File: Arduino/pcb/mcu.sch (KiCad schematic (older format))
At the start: 25 parts, among them J9 FTDI, SW2 Reset Button, U2 ATMEGA328P-AU, U3 24LC64, Y1 20 Mhz Crystal

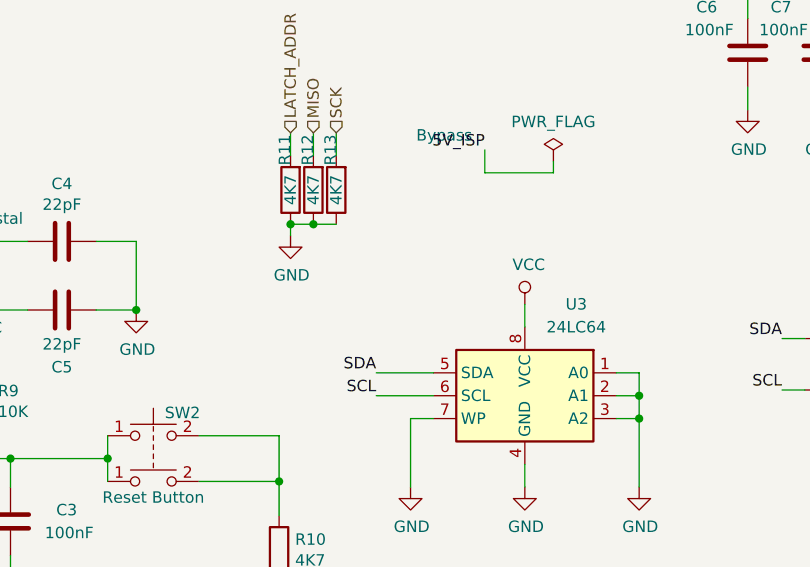
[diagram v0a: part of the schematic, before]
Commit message: pcb: mcu: add and route I2C pull up resistors
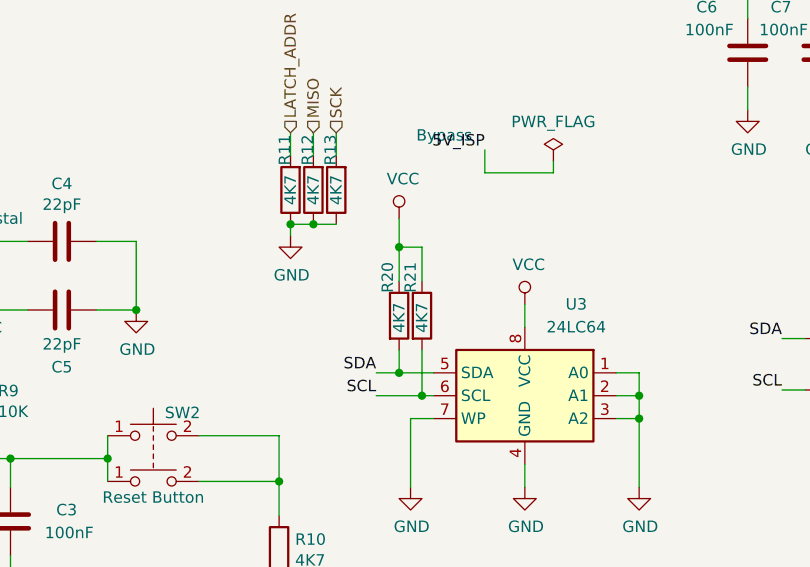
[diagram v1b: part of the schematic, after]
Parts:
- added R20, R21: 4K7, Resistor_SMD:R_0805_2012Metric, symbol Device:R
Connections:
- net SCL: now also R21.2
- net SDA: now also R20.2
- net VCC: now also R20.1, R21.1
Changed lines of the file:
@@
 RESET
 Wire Wire Line
-	8425 3550 8675 3550
-Wire Wire Line
-	8425 3650 8675 3650
+	8425 3550 8525 3550
 $Bitmap
 Pos 2000 2125
@@
 EndData
 $EndBitmap
+$Comp
+L Device:R R21
+U 1 1 5D785D49
+P 8625 3300
+F 0 "R21" V 8575 3400 50  0000 L CNN
+F 1 "4K7" V 8625 3225 50  0000 L CNN
+F 2 "Resistor_SMD:R_0805_2012Metric" V 8555 3300 50  0001 C CNN
+F 3 "~" H 8625 3300 50  0001 C CNN
+	1    8625 3300
+	1    0    0    -1
+$EndComp
+$Comp
+L Device:R R20
+U 1 1 5D78678B
+P 8525 3300
+F 0 "R20" V 8475 3400 50  0000 L CNN
+F 1 "4K7" V 8525 3225 50  0000 L CNN
+F 2 "Resistor_SMD:R_0805_2012Metric" V 8455 3300 50  0001 C CNN
+F 3 "~" H 8525 3300 50  0001 C CNN
+	1    8525 3300
+	1    0    0    -1
+$EndComp
+Wire Wire Line
+	8625 3450 8625 3650
+Connection ~ 8625 3650
+Wire Wire Line
+	8625 3650 8675 3650
+Wire Wire Line
+	8425 3650 8625 3650
+Wire Wire Line
+	8525 3450 8525 3550
+Connection ~ 8525 3550
+Wire Wire Line
+	8525 3550 8675 3550
+Wire Wire Line
+	8525 3150 8525 3000
+Wire Wire Line
+	8625 3150 8625 3000
+Wire Wire Line
+	8625 3000 8525 3000
+Wire Wire Line
+	8525 3000 8525 2875
+Connection ~ 8525 3000
+$Comp
+L power:VCC #PWR0101
+U 1 1 5D7ACF72
+P 8525 2875
+F 0 "#PWR0101" H 8525 2725 50  0001 C CNN
+F 1 "VCC" H 8542 3048 50  0000 C CNN
+F 2 "" H 8525 2875 50  0001 C CNN
+F 3 "" H 8525 2875 50  0001 C CNN
+	1    8525 2875
+	1    0    0    -1
+$EndComp
 $EndSCHEMATC

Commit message: pcb: use OR gate between FTDI and RS485 TX lines
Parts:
- added U5: 74AHCT1G32, Package_TO_SOT_SMD:SOT-23-5, symbol 74xGxx:74AHCT1G32
- R7, R8: value 100R -> 4k7
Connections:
- wire segments 109 -> 116
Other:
- moved on the sheet: C3
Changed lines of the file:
@@
 	7650 4025 8000 4025
 $Comp
-L Device:C C3
-U 1 1 5CCED101
-P 6825 4200
-F 0 "C3" H 7025 4250 50  0000 L CNN
-F 1 "100nF" H 6975 4150 50  0000 L CNN
-F 2 "Capacitor_SMD:C_0805_2012Metric" H 6863 4050 50  0001 C CNN
-F 3 "~" H 6825 4200 50  0001 C CNN
-	1    6825 4200
-	1    0    0    -1
-$EndComp
-$Comp
 L Device:R R10
 U 1 1 5CCED110
@@
 Wire Wire Line
 	8000 4525 8000 4475
-Wire Wire Line
-	7400 4850 6825 4850
-Connection ~ 6825 3925
 Text HLabel 7225 5150 0    50   Output ~ 0
 5V_ISP
@@
 	5825 3925 6500 3925
 Wire Wire Line
-	6825 3925 7250 3925
-Wire Wire Line
 	6700 3825 6700 3925
 Connection ~ 6700 3925
-Wire Wire Line
-	6700 3925 6825 3925
 Connection ~ 7375 3275
-Wire Wire Line
-	6825 3925 6825 4050
-Text HLabel 6325 5050 0    50   Input ~ 0
-RX
-Text HLabel 6325 4950 0    50   Output ~ 0
+Text HLabel 5950 5100 0    50   Output ~ 0
 TX
 Wire Wire Line
-	6825 4350 6825 4850
-Wire Wire Line
-	5825 4175 6425 4175
-Wire Wire Line
-	6525 4075 5825 4075
-Wire Wire Line
-	7400 5050 6625 5050
-Wire Wire Line
-	6625 5050 6625 4450
-Wire Wire Line
-	6675 4350 6675 4950
-Wire Wire Line
-	7400 4950 6675 4950
-Wire Wire Line
-	6325 4950 6425 4950
-Wire Wire Line
-	6325 5050 6525 5050
-$Comp
-L Device:R R7
-U 1 1 5CFC6CB8
-P 6425 4700
-F 0 "R7" H 6275 4850 50  0000 L CNN
-F 1 "100R" V 6425 4600 50  0000 L CNN
-F 2 "Resistor_SMD:R_0805_2012Metric" V 6355 4700 50  0001 C CNN
-F 3 "~" H 6425 4700 50  0001 C CNN
-	1    6425 4700
-	1    0    0    -1
-$EndComp
-Wire Wire Line
-	6425 4950 6425 4850
-$Comp
-L Device:R R8
-U 1 1 5CFCA336
-P 6525 4700
-F 0 "R8" H 6425 4850 50  0000 L CNN
-F 1 "100R" V 6525 4600 50  0000 L CNN
-F 2 "Resistor_SMD:R_0805_2012Metric" V 6455 4700 50  0001 C CNN
-F 3 "~" H 6525 4700 50  0001 C CNN
-	1    6525 4700
-	1    0    0    -1
-$EndComp
-Wire Wire Line
-	6525 5050 6525 4850
+	5825 4175 6050 4175
 $Comp
 L Device:C C?
@@
 	9200 2625 9200 2675
 Wire Wire Line
-	6425 4175 6425 4350
-Wire Wire Line
-	6525 4075 6525 4450
-Wire Wire Line
-	6675 4350 6425 4350
-Connection ~ 6425 4350
-Wire Wire Line
-	6425 4350 6425 4550
-Wire Wire Line
-	6625 4450 6525 4450
-Connection ~ 6525 4450
-Wire Wire Line
-	6525 4450 6525 4550
-Wire Wire Line
 	8250 2900 8150 2900
 Wire Wire Line
@@
 	1    0    0    -1
 $EndComp
+$Comp
+L 74xGxx:74AHCT1G32 U5
+U 1 1 5D9A3C33
+P 6425 5100
+F 0 "U5" H 6375 5250 50  0000 R CNN
+F 1 "74AHCT1G32" H 6675 4925 50  0000 R CNN
+F 2 "Package_TO_SOT_SMD:SOT-23-5" H 6425 5100 50  0001 C CNN
+F 3 "http://www.ti.com/lit/sg/scyt129e/scyt129e.pdf" H 6425 5100 50  0001 C CNN
+	1    6425 5100
+	-1   0    0    -1
+$EndComp
+$Comp
+L power:GND #PWR047
+U 1 1 5D9DCC48
+P 6425 5300
+F 0 "#PWR047" H 6425 5050 50  0001 C CNN
+F 1 "GND" H 6430 5127 50  0000 C CNN
+F 2 "" H 6425 5300 50  0001 C CNN
+F 3 "" H 6425 5300 50  0001 C CNN
+	1    6425 5300
+	-1   0    0    -1
+$EndComp
+$Comp
+L power:VCC #PWR046
+U 1 1 5D9E0DFB
+P 6425 4900
+F 0 "#PWR046" H 6425 4750 50  0001 C CNN
+F 1 "VCC" H 6442 5073 50  0000 C CNN
+F 2 "" H 6425 4900 50  0001 C CNN
+F 3 "" H 6425 4900 50  0001 C CNN
+	1    6425 4900
+	-1   0    0    -1
+$EndComp
+Text HLabel 5950 5225 0    50   Input ~ 0
+RX
+Connection ~ 6050 4175
+Wire Wire Line
+	5950 5100 6050 5100
+Wire Wire Line
+	6050 4175 6050 5100
+Wire Wire Line
+	5825 4075 6125 4075
+Wire Wire Line
+	6125 4075 6125 5100
+Wire Wire Line
+	6125 5100 6175 5100
+$Comp
+L Device:R R7
+U 1 1 5D96B9DF
+P 6725 4750
+F 0 "R7" V 6650 4875 50  0000 L CNN
+F 1 "4k7" V 6725 4675 50  0000 L CNN
+F 2 "Resistor_SMD:R_0805_2012Metric" V 6655 4750 50  0001 C CNN
+F 3 "~" H 6725 4750 50  0001 C CNN
+	1    6725 4750
+	1    0    0    -1
+$EndComp
+$Comp
+L Device:R R8
+U 1 1 5D973982
+P 6825 4750
+F 0 "R8" V 6775 4875 50  0000 L CNN
+F 1 "4k7" V 6825 4675 50  0000 L CNN
+F 2 "Resistor_SMD:R_0805_2012Metric" V 6755 4750 50  0001 C CNN
+F 3 "~" H 6825 4750 50  0001 C CNN
+	1    6825 4750
+	1    0    0    -1
+$EndComp
+Wire Wire Line
+	6425 5000 6425 4900
+Wire Wire Line
+	6425 5200 6425 5300
+Wire Wire Line
+	6725 5575 6050 5575
+Wire Wire Line
+	6050 5575 6050 5225
+Wire Wire Line
+	6050 5225 5950 5225
+Wire Wire Line
+	6725 5150 6725 5575
+$Comp
+L Device:C C3
+U 1 1 5CCED101
+P 7150 4250
+F 0 "C3" H 7350 4300 50  0000 L CNN
+F 1 "100nF" H 7300 4200 50  0000 L CNN
+F 2 "Capacitor_SMD:C_0805_2012Metric" H 7188 4100 50  0001 C CNN
+F 3 "~" H 7150 4250 50  0001 C CNN
+	1    7150 4250
+	1    0    0    -1
+$EndComp
+Wire Wire Line
+	6050 4175 7000 4175
+Wire Wire Line
+	7150 4100 7150 3925
+Connection ~ 7150 3925
+Wire Wire Line
+	7150 3925 7250 3925
+Wire Wire Line
+	6700 3925 7150 3925
+$Comp
+L power:VCC #PWR048
+U 1 1 5DA39DEA
+P 6825 4450
+F 0 "#PWR048" H 6825 4300 50  0001 C CNN
+F 1 "VCC" H 6842 4623 50  0000 C CNN
+F 2 "" H 6825 4450 50  0001 C CNN
+F 3 "" H 6825 4450 50  0001 C CNN
+	1    6825 4450
+	1    0    0    -1
+$EndComp
+Wire Wire Line
+	6825 4600 6825 4500
+Wire Wire Line
+	6725 4600 6725 4500
+Wire Wire Line
+	6725 4500 6825 4500
+Connection ~ 6825 4500
+Wire Wire Line
+	6825 4500 6825 4450
+Wire Wire Line
+	7000 4950 7400 4950
+Wire Wire Line
+	7000 4175 7000 4950
+Wire Wire Line
+	7150 4850 7400 4850
+Wire Wire Line
+	7150 4400 7150 4850
+Connection ~ 6725 5050
+Wire Wire Line
+	6725 5050 7400 5050
+Wire Wire Line
+	6725 5150 6825 5150
+Connection ~ 6725 5150
+Wire Wire Line
+	6725 4900 6725 5050
+Wire Wire Line
+	6825 4900 6825 5150
 $EndSCHEMATC

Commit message: pcb: mcu: replace OR by AND gate / use pullups on TX pins
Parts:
- removed U5: 74AHCT1G32, Package_TO_SOT_SMD:SOT-23-5, symbol 74xGxx:74AHCT1G32
- added U5: 74AHC1G08, Package_TO_SOT_SMD:SOT-23-5, symbol 74xGxx:74AHC1G08
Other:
- moved on the sheet: C6, C7, R10, R11, R12, R13, R20, R21, SW2, TP1, TP2, TP3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

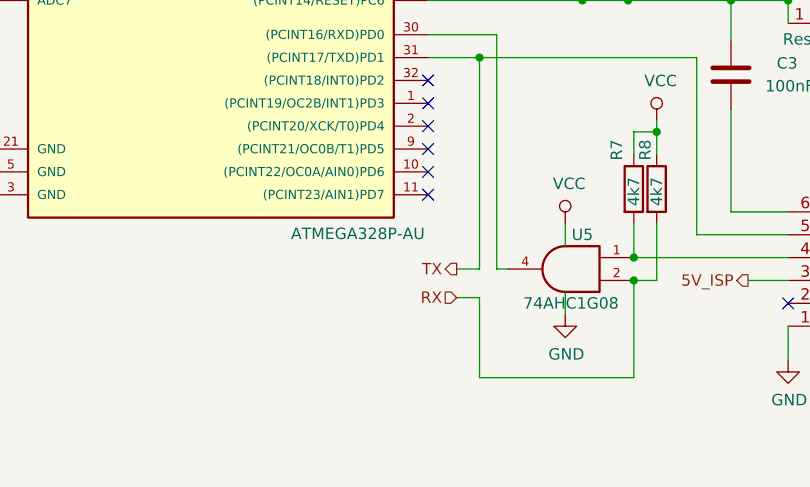
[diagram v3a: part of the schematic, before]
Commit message: pcb: mcu / bus: improve TX/RX labels for RS485 transceiver
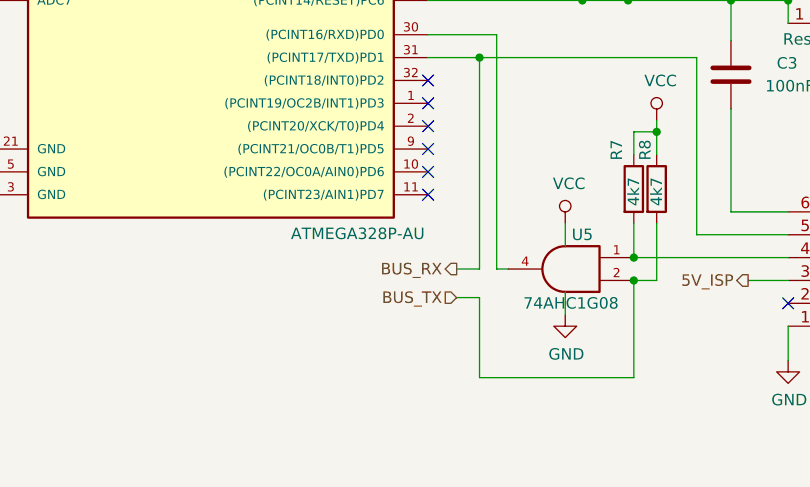
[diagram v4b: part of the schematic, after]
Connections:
- net RX renamed BUS_TX
- net TX renamed BUS_RX
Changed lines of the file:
@@
 $Descr A4 11693 8268
 encoding utf-8
-Sheet 5 6
+Sheet 6 6
 Title ""
 Date ""
@@
 Connection ~ 6700 3925
 Connection ~ 7375 3275
-Text HLabel 5950 5100 0    50   Output ~ 0
-TX
 Wire Wire Line
 	5825 4175 6050 4175
@@
 	1    0    0    -1
 $EndComp
-Text HLabel 5950 5225 0    50   Input ~ 0
-RX
 Connection ~ 6050 4175
 Wire Wire Line
@@
 	1    0    0    -1
 $EndComp
+Text HLabel 5950 5225 0    50   Input ~ 0
+BUS_TX
+Text HLabel 5950 5100 0    50   Output ~ 0
+BUS_RX
 $EndSCHEMATC

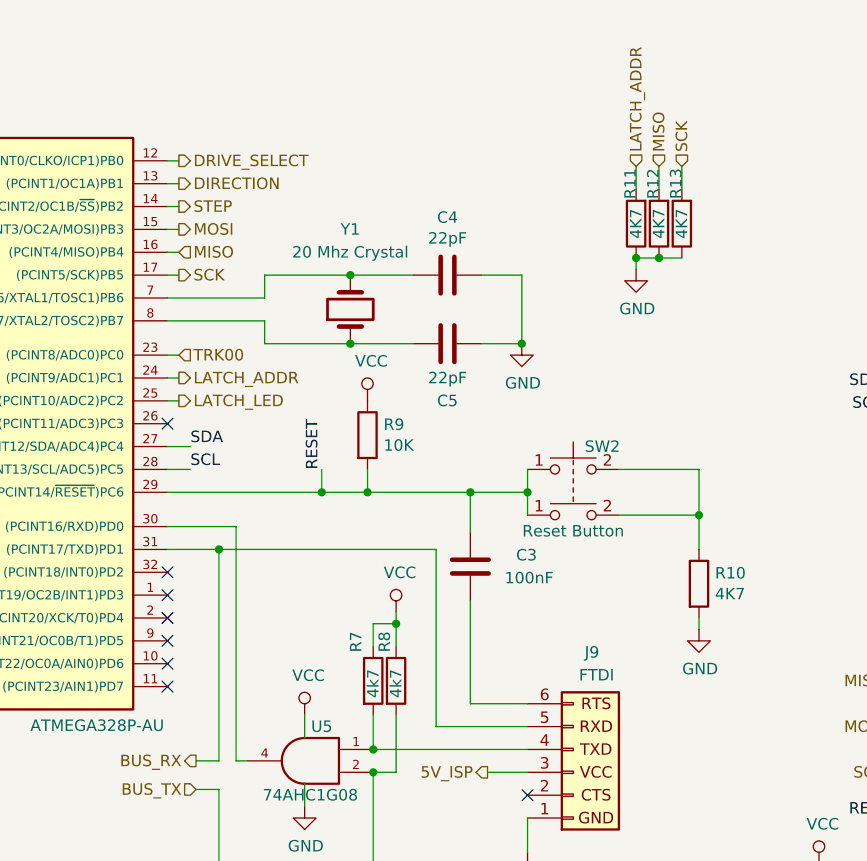
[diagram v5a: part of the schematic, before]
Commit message: pcb / floppy: remove 4094 shift register / connect address connector directly
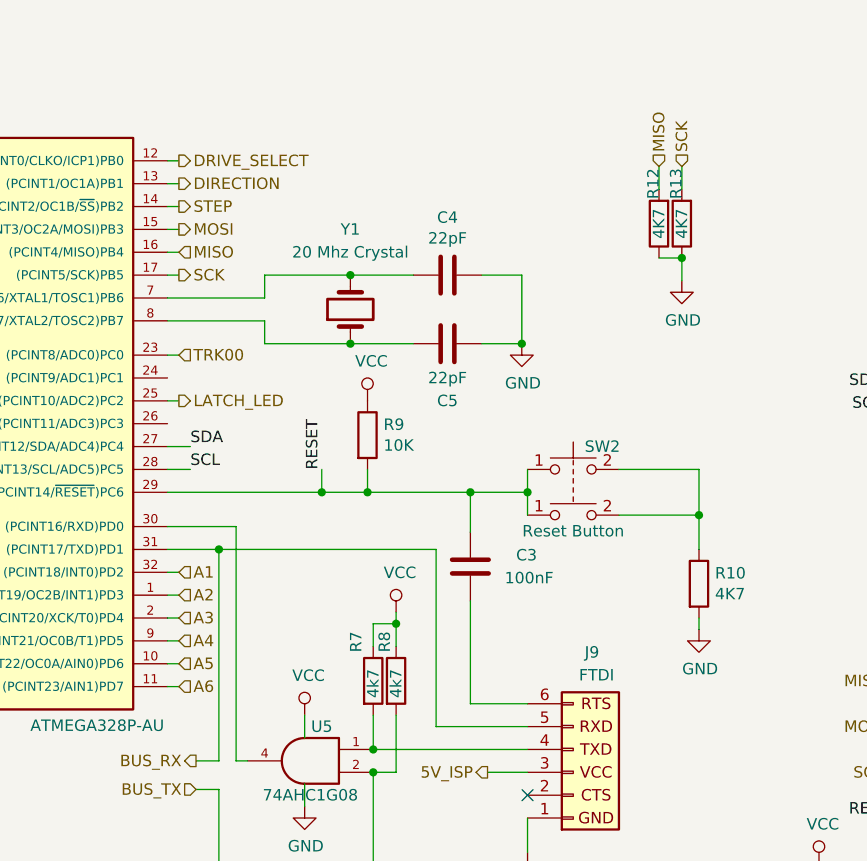
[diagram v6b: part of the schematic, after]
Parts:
- removed R11: 4K7, Resistor_SMD:R_0805_2012Metric, symbol Device:R
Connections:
- net A2: now reaches U2.1 ((PCINT19/OC2B/INT1)PD3)
- net A5: now reaches U2.10 ((PCINT22/OC0A/AIN0)PD6)
- net A6: now reaches U2.11 ((PCINT23/AIN1)PD7)
- net A3: now reaches U2.2 ((PCINT20/XCK/T0)PD4)
- net A1: now reaches U2.32 ((PCINT18/INT0)PD2)
- net A4: now reaches U2.9 ((PCINT21/OC0B/T1)PD5)
- net LATCH_ADDR: no longer names the net of U2.24 ((PCINT9/ADC1)PC1)
- no-connect marks 11 -> 4
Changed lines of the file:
@@
 Comment4 ""
 $EndDescr
-NoConn ~ 5825 3625
-NoConn ~ 5825 4775
-NoConn ~ 5825 4675
-NoConn ~ 5825 4575
-NoConn ~ 5825 4475
-NoConn ~ 5825 4375
-NoConn ~ 5825 4275
 NoConn ~ 3925 3925
 NoConn ~ 3925 3825
@@
 	6250 3175 6250 3275
 Wire Wire Line
-	5825 3425 5875 3425
-Wire Wire Line
 	5825 3325 5875 3325
 Wire Wire Line
@@
 	0    -1   -1   0
 $EndComp
-$Comp
-L floppyorgel-rescue:ATMEGA328P-AU-atmel U?
-U 1 1 5CC6668C
-P 4825 3575
-AR Path="/5CC6668C" Ref="U?"  Part="1"
-AR Path="/5CCFEC3E/5CC6668C" Ref="U2"  Part="1"
-F 0 "U2" H 4075 4825 50  0000 L BNN
-F 1 "ATMEGA328P-AU" H 5225 2175 50  0000 L BNN
-F 2 "Package_QFP:LQFP-32_7x7mm_P0.8mm" H 4825 3575 50  0001 C CIN
-F 3 "" H 4825 3575 50  0001 C CNN
-	1    4825 3575
-	1    0    0    -1
-$EndComp
 Text HLabel 5875 2475 2    50   Output ~ 0
 DRIVE_SELECT
@@
 Text HLabel 5875 3325 2    50   Input ~ 0
 TRK00
-Text HLabel 5875 3425 2    50   Output ~ 0
-LATCH_ADDR
-Text HLabel 5875 3525 2    50   Output ~ 0
-LATCH_LED
 $Comp
 L ftdi:FTDI J9
@@
 Bypass
 Wire Wire Line
-	7875 2500 7875 2600
-Wire Wire Line
 	8075 2500 8075 2600
 Wire Wire Line
 	7975 2500 7975 2600
-Wire Wire Line
-	7875 2900 7875 2950
-$Comp
-L power:GND #PWR?
-U 1 1 5D158700
-P 7875 2950
-AR Path="/5D158700" Ref="#PWR?"  Part="1"
-AR Path="/5CCFEC3E/5D158700" Ref="#PWR025"  Part="1"
-F 0 "#PWR025" H 7875 2700 50  0001 C CNN
-F 1 "GND" H 7880 2777 50  0000 C CNN
-F 2 "" H 7875 2950 50  0001 C CNN
-F 3 "" H 7875 2950 50  0001 C CNN
-	1    7875 2950
-	1    0    0    -1
-$EndComp
-Text HLabel 7875 2500 1    50   Input ~ 0
-LATCH_ADDR
 Text HLabel 7975 2500 1    50   Input ~ 0
 MISO
@@
 	-1   0    0    1
 $EndComp
-$Comp
-L Device:R R?
-U 1 1 5D1586DC
-P 7875 2750
-AR Path="/5D1586DC" Ref="R?"  Part="1"
-AR Path="/5CCFEC3E/5D1586DC" Ref="R11"  Part="1"
-F 0 "R11" V 7900 2575 50  0000 C CNN
-F 1 "4K7" V 7875 2750 50  0000 C CNN
-F 2 "Resistor_SMD:R_0805_2012Metric" V 7805 2750 50  0001 C CNN
-F 3 "~" H 7875 2750 50  0001 C CNN
-	1    7875 2750
-	-1   0    0    1
-$EndComp
 NoConn ~ 3925 3075
 $Comp
@@
 Wire Wire Line
 	8075 2900 7975 2900
-Wire Wire Line
-	7975 2900 7875 2900
-Connection ~ 7975 2900
-Connection ~ 7875 2900
 $Comp
 L Memory_EEPROM:24LC64 U3
@@
 	1    0    0    -1
 $EndComp
+Text HLabel 5875 4375 2    50   Input ~ 0
+A2
+Text HLabel 5875 4475 2    50   Input ~ 0
+A3
+Text HLabel 5875 4575 2    50   Input ~ 0
+A4
+Text HLabel 5875 4675 2    50   Input ~ 0
+A5
+Text HLabel 5875 4775 2    50   Input ~ 0
+A6
+$Comp
+L floppyorgel-rescue:ATMEGA328P-AU-atmel U?
+U 1 1 5CC6668C
+P 4825 3575
+AR Path="/5CC6668C" Ref="U?"  Part="1"
+AR Path="/5CCFEC3E/5CC6668C" Ref="U2"  Part="1"
+F 0 "U2" H 4075 4825 50  0000 L BNN
+F 1 "ATMEGA328P-AU" H 5225 2175 50  0000 L BNN
+F 2 "Package_QFP:LQFP-32_7x7mm_P0.8mm" H 4825 3575 50  0001 C CIN
+F 3 "" H 4825 3575 50  0001 C CNN
+	1    4825 3575
+	1    0    0    -1
+$EndComp
+Wire Wire Line
+	5825 4375 5875 4375
+Wire Wire Line
+	5825 4475 5875 4475
+Wire Wire Line
+	5825 4575 5875 4575
+Wire Wire Line
+	5825 4675 5875 4675
+Wire Wire Line
+	5825 4775 5875 4775
+Wire Wire Line
+	5825 4275 5875 4275
+Text HLabel 5875 4275 2    50   Input ~ 0
+A1
+Text HLabel 5875 3525 2    50   Output ~ 0
+LATCH_LED
+$Comp
+L power:GND #PWR?
+U 1 1 5D158700
+P 8075 3000
+AR Path="/5D158700" Ref="#PWR?"  Part="1"
+AR Path="/5CCFEC3E/5D158700" Ref="#PWR025"  Part="1"
+F 0 "#PWR025" H 8075 2750 50  0001 C CNN
+F 1 "GND" H 8080 2827 50  0000 C CNN
+F 2 "" H 8075 3000 50  0001 C CNN
+F 3 "" H 8075 3000 50  0001 C CNN
+	1    8075 3000
+	1    0    0    -1
+$EndComp
+Wire Wire Line
+	8075 2900 8075 3000
+Connection ~ 8075 2900
 $EndSCHEMATC
